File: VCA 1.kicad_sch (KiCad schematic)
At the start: 58 parts, among them J1 Eurorack 2x8hs, J15 IN 1x8s, J2 LED 1x3s, J3 CV 1x5s, J4 OUT 1x2s, U1 TL074, U2 AS2164

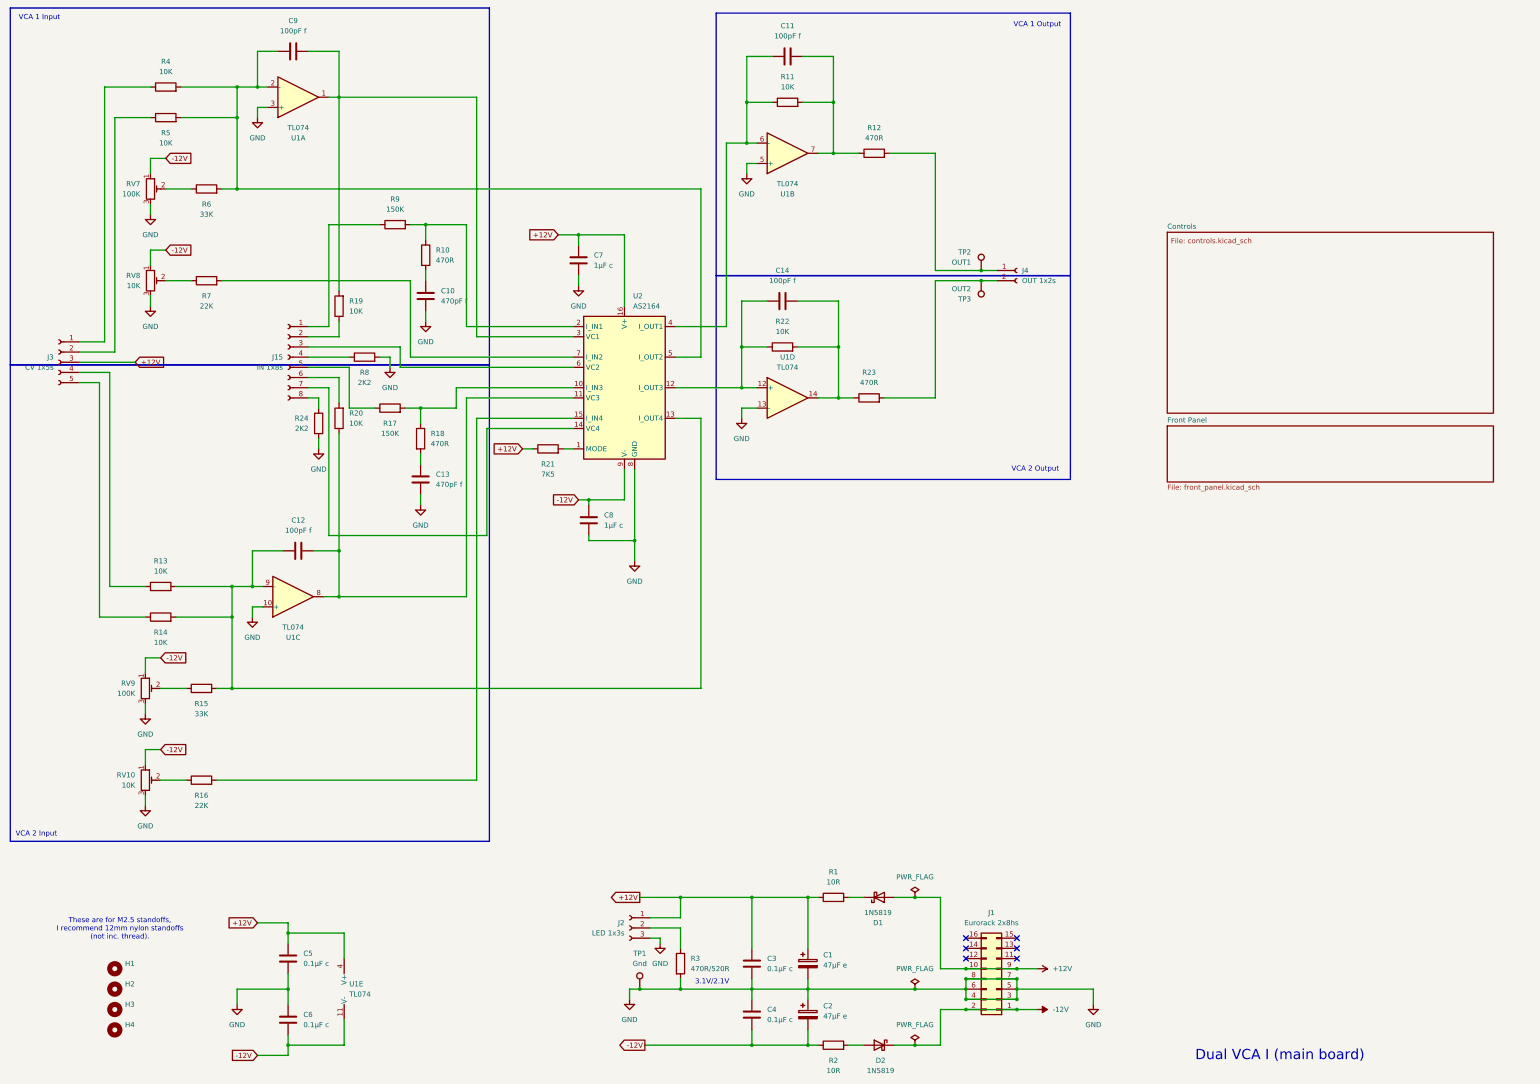
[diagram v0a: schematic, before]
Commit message: Updated schematic and .gitignore
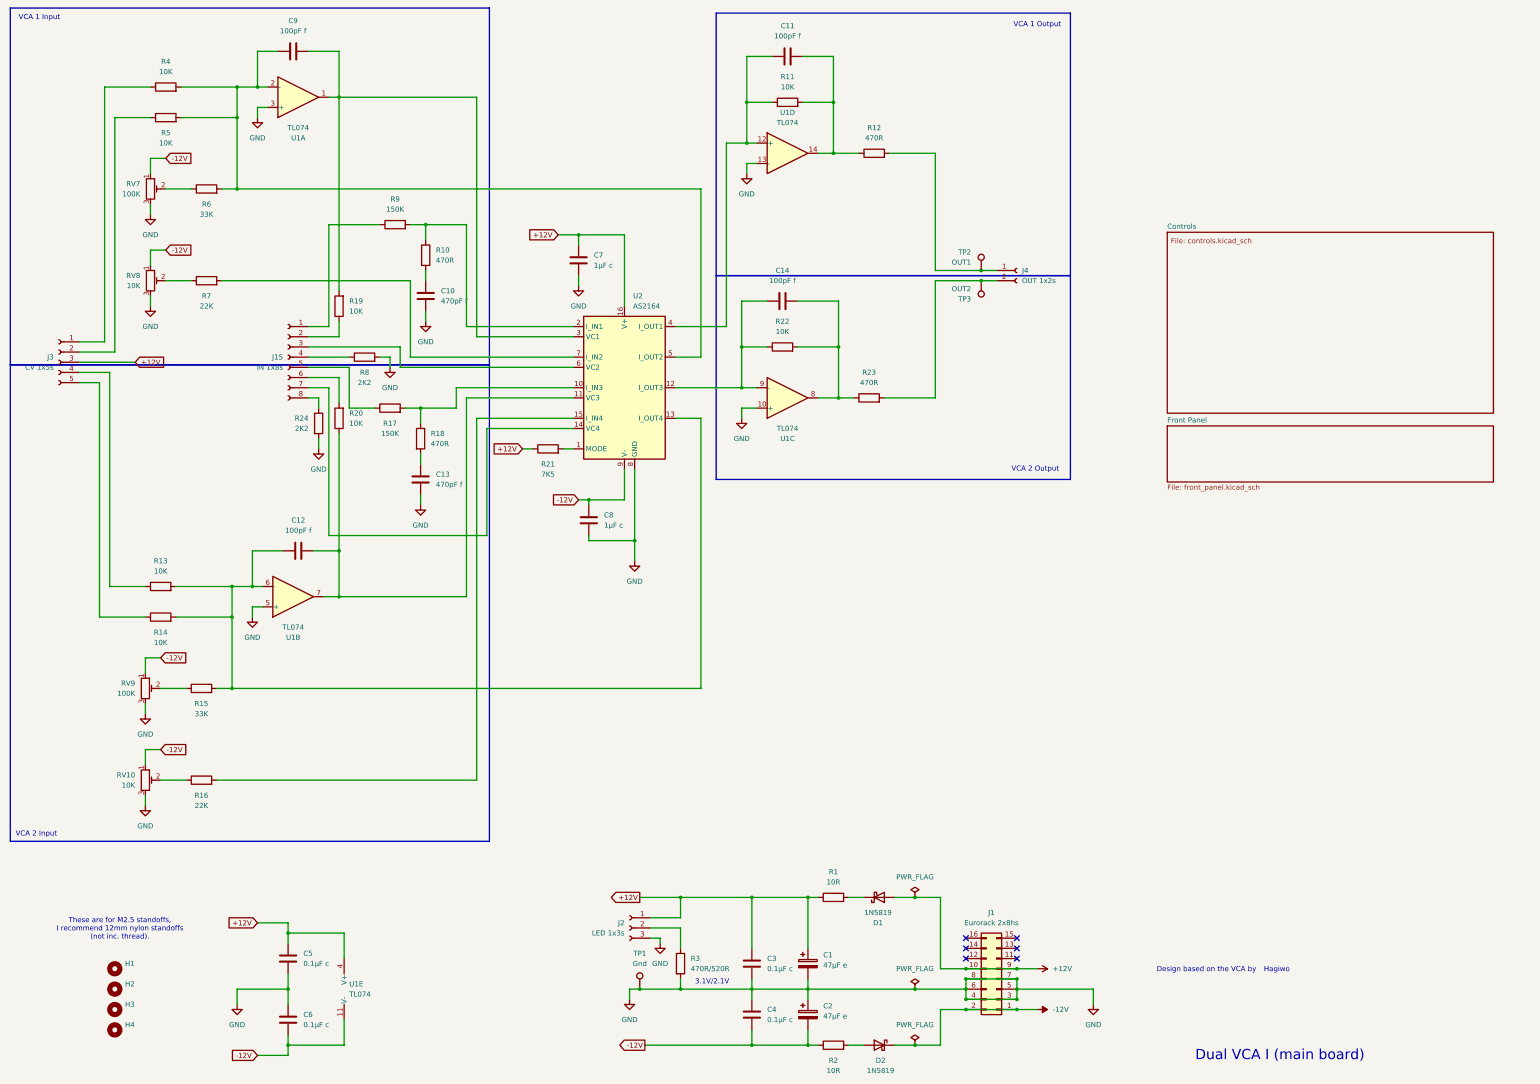
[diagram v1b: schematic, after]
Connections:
- net at C11.1, R11.1, U2.4 (I_OUT1): now also U1.12 (+); no longer U1.6 (-)
- net at C11.2, R11.2, R12.1: now also U1.14; no longer U1.7
- net at C12.2, R20.1, U2.11 (VC3): now also U1.7; no longer U1.8
- net at C14.1, R22.1, U2.12 (I_OUT3): now also U1.9 (-); no longer U1.12 (+)
- net at C12.1, R13.2, R14.2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: now also U1.6 (-); no longer U1.9 (-)
- net at C14.2, R22.2, R23.1: now also U1.8; no longer U1.14
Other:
- note added: "Design based on the VCA by"
- note added: "Hagiwo"

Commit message: Added input LED
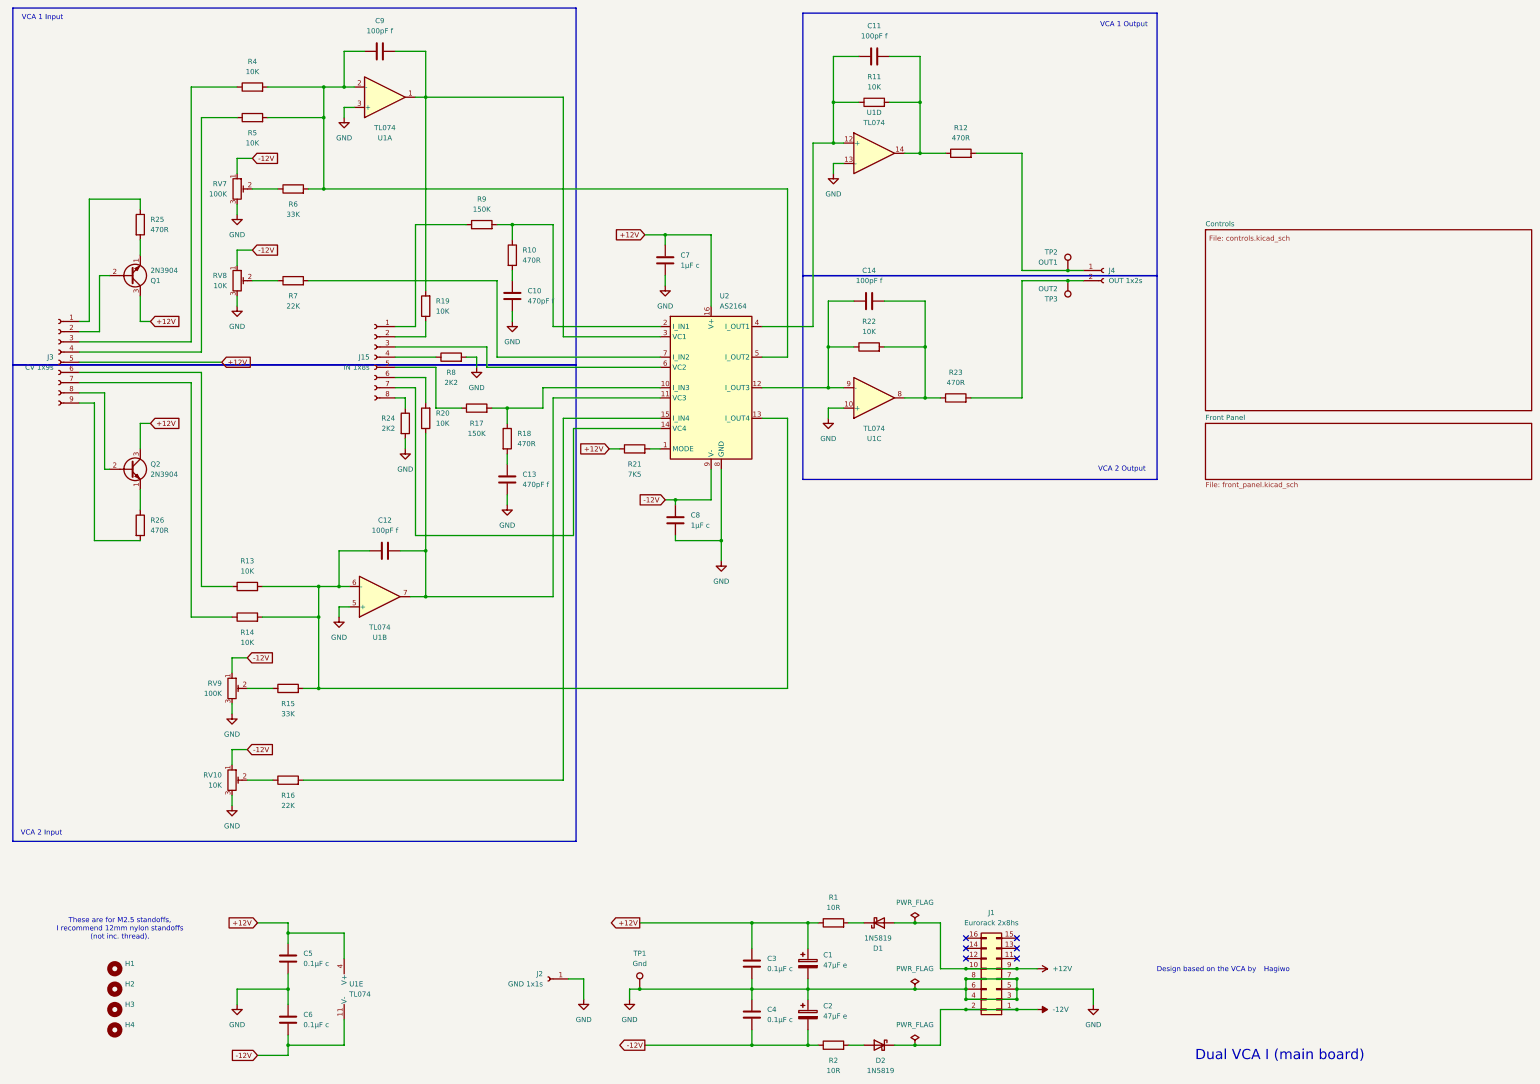
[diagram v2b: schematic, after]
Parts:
- removed J2: LED 1x3s, symbol Connector:Conn_01x03_Socket
- removed J3: CV 1x5s, symbol Connector:Conn_01x05_Socket
- removed R3: 470R/520R, Resistor_THT:R_Axial_DIN0204_L3.6mm_D1.6mm_P2.54mm_Vertical, symbol Device:R
- added J2: GND 1x1s, symbol Connector:Conn_01x01_Socket
- added J3: CV 1x9s, symbol Connector:Conn_01x09_Socket
- added Q1, Q2: 2N3904, Package_TO_SOT_THT:TO-92_Inline, symbol Transistor_BJT:2N3904
- added R25, R26: 470R, symbol Device:R
- C7, C8: footprint (none) -> Capacitor_THT:C_Disc_D4.7mm_W2.5mm_P5.00mm
- U1: footprint (none) -> Package_DIP:DIP-14_W7.62mm
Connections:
- net +12V: now also J3.5 (Pin_5), Q1.3 (C), Q2.3 (C)
- net GND: now also J2.1 (Pin_1)
- net at R4.1: now also J3.3 (Pin_3)
- net at R14.1: now also J3.7 (Pin_7)
- net at R5.1: now also J3.4 (Pin_4)
- net at R13.1: now also J3.6 (Pin_6)
- new net: J3.1 (Pin_1), R25.1
- new net: Q1.1 (E), R25.2
- new net: J3.2 (Pin_2), Q1.2 (B)
- new net: J3.8 (Pin_8), Q2.2 (B)
- new net: J3.9 (Pin_9), R26.2
- new net: Q2.1 (E), R26.1
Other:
- note removed: "3.1V/2.1V"
- moved on the sheet: C10, C11, C12, C13, C14, C7, C8, C9, D1, J15, J4, R1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

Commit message: Added test points and calibration information.
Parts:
- added TP4: IN1, TestPoint:TestPoint_Loop_D2.50mm_Drill1.0mm, symbol Connector:TestPoint
- added TP5: IN2, TestPoint:TestPoint_Loop_D2.50mm_Drill1.0mm, symbol Connector:TestPoint
- added TP6: CV1, TestPoint:TestPoint_Loop_D2.50mm_Drill1.0mm, symbol Connector:TestPoint
- added TP7: CV2, TestPoint:TestPoint_Loop_D2.50mm_Drill1.0mm, symbol Connector:TestPoint
- R4: footprint (none) -> Resistor_THT:R_Axial_DIN0204_L3.6mm_D1.6mm_P7.62mm_Horizontal
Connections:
- net at J15.1 (Pin_1), R9.1: now also TP4.1
- net at J15.5 (Pin_5), R17.1: now also TP5.1
- net at J3.2 (Pin_2), Q1.2 (B): now also TP6.1
- net at J3.8 (Pin_8), Q2.2 (B): now also TP7.1
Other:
- moved on the sheet: C13, R10, R17, R18, R20, R9

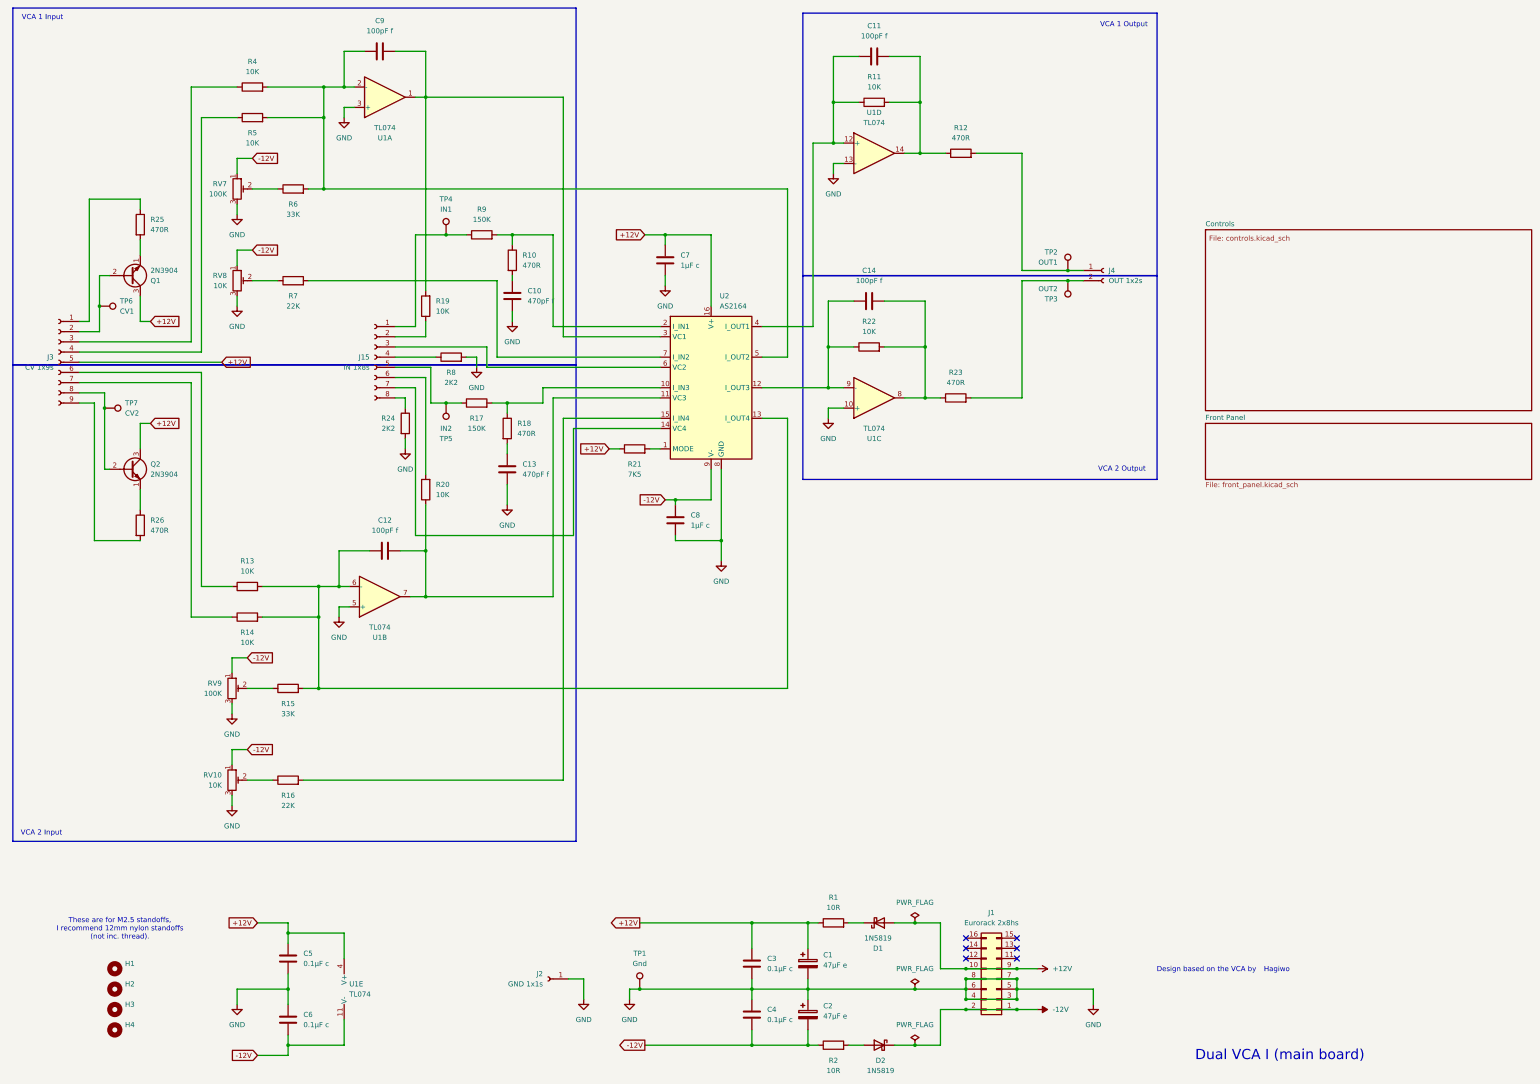
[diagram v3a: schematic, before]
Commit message: Started on the PCB layout
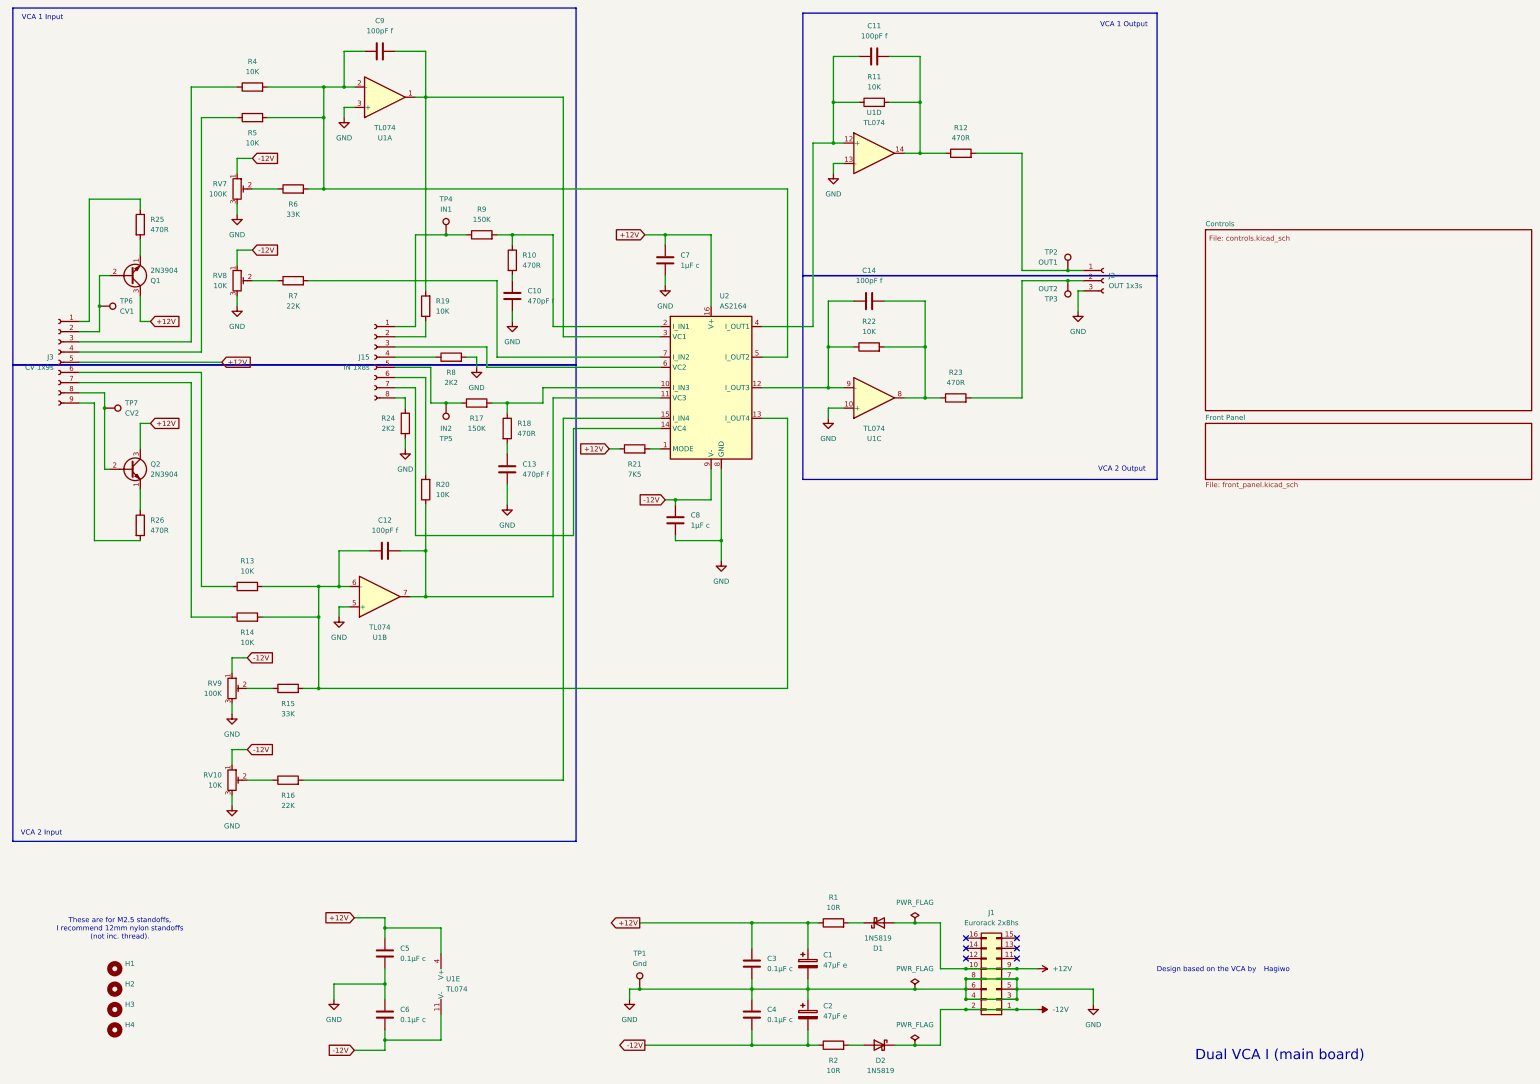
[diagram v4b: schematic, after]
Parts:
- removed J2: GND 1x1s, symbol Connector:Conn_01x01_Socket
- removed J4: OUT 1x2s, symbol Connector:Conn_01x02_Socket
- added J2: OUT 1x3s, Connector_PinSocket_2.54mm:PinSocket_1x03_P2.54mm_Vertical, symbol Connector:Conn_01x03_Socket
- C10, C11, C12, C13, C14, C9: footprint (none) -> Capacitor_THT:C_Rect_L7.2mm_W2.5mm_P5.00mm
- J1: footprint Connector_PinHeader_2.54mm:PinHeader_2x08_P2.54mm_Vertical -> Connector_IDC:IDC-Header_2x08_P2.54mm_Vertical
- J15: footprint (none) -> Connector_PinSocket_2.54mm:PinSocket_1x08_P2.54mm_Vertical
- J3: footprint (none) -> Connector_PinSocket_2.54mm:PinSocket_1x09_P2.54mm_Vertical
- R10, R11, R12, R16, R17, R19, R21, R22, R24, R25, R26, R8, R9: footprint (none) -> Resistor_THT:R_Axial_DIN0204_L3.6mm_D1.6mm_P2.54mm_Vertical
- R13, R14, R15, R18, R20, R23, R5, R6, R7: footprint (none) -> Resistor_THT:R_Axial_DIN0204_L3.6mm_D1.6mm_P7.62mm_Horizontal
- RV10, RV7, RV8, RV9: footprint (none) -> Potentiometer_THT:Potentiometer_Bourns_3296W_Vertical
- U2: footprint Package_SO:SOIC-16_3.9x9.9mm_P1.27mm -> Package_DIP:DIP-16_W7.62mm
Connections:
- net GND: now also J2.3 (Pin_3)
- net at R12.2, TP2.1: now also J2.1 (Pin_1)
- net at R23.2, TP3.1: now also J2.2 (Pin_2)
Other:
- moved on the sheet: C5, C6, U1E

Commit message: PCB passes EDC and panel cutouts done
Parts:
- Q1, Q2: footprint Package_TO_SOT_THT:TO-92_Inline -> Package_TO_SOT_THT:TO-92_Inline_Wide
- R12: footprint Resistor_THT:R_Axial_DIN0204_L3.6mm_D1.6mm_P2.54mm_Vertical -> Resistor_THT:R_Axial_DIN0204_L3.6mm_D1.6mm_P7.62mm_Horizontal
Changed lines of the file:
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@@
 			)
 		)
-		(property "Footprint" "Package_TO_SOT_THT:TO-92_Inline"
+		(property "Footprint" "Package_TO_SOT_THT:TO-92_Inline_Wide"
 			(at 52.07 132.715 0)
 			(hide yes)
@@
 			)
 		)
-		(property "Footprint" "Package_TO_SOT_THT:TO-92_Inline"
+		(property "Footprint" "Package_TO_SOT_THT:TO-92_Inline_Wide"
 			(at 52.07 80.645 0)
 			(hide yes)
@@
 			)
 		)
-		(property "Footprint" "Resistor_THT:R_Axial_DIN0204_L3.6mm_D1.6mm_P2.54mm_Vertical"
+		(property "Footprint" "Resistor_THT:R_Axial_DIN0204_L3.6mm_D1.6mm_P7.62mm_Horizontal"
 			(at 254 53.848 90)
 			(hide yes)
